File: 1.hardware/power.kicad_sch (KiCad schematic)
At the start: 45 parts, among them IC1 TPS7A2033PDBVR, IC4 TPS7A2018PDBVR, IC5 LMR14030SDDAR, J4 12V~24V BAT, J5 12V-24V Jack

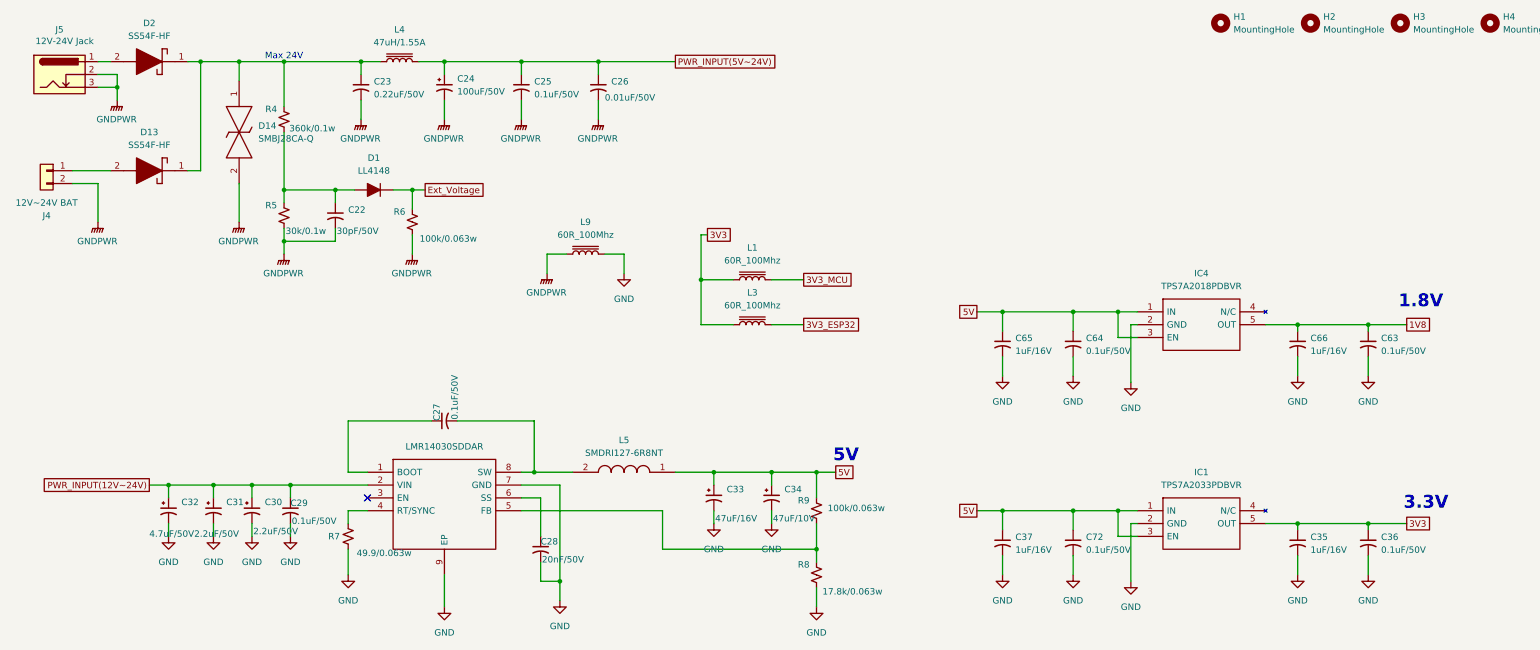
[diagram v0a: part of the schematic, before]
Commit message: 스펙 변경 12~48V 인풋 + 모스펫 구동에 필요한 전압 구현 필요
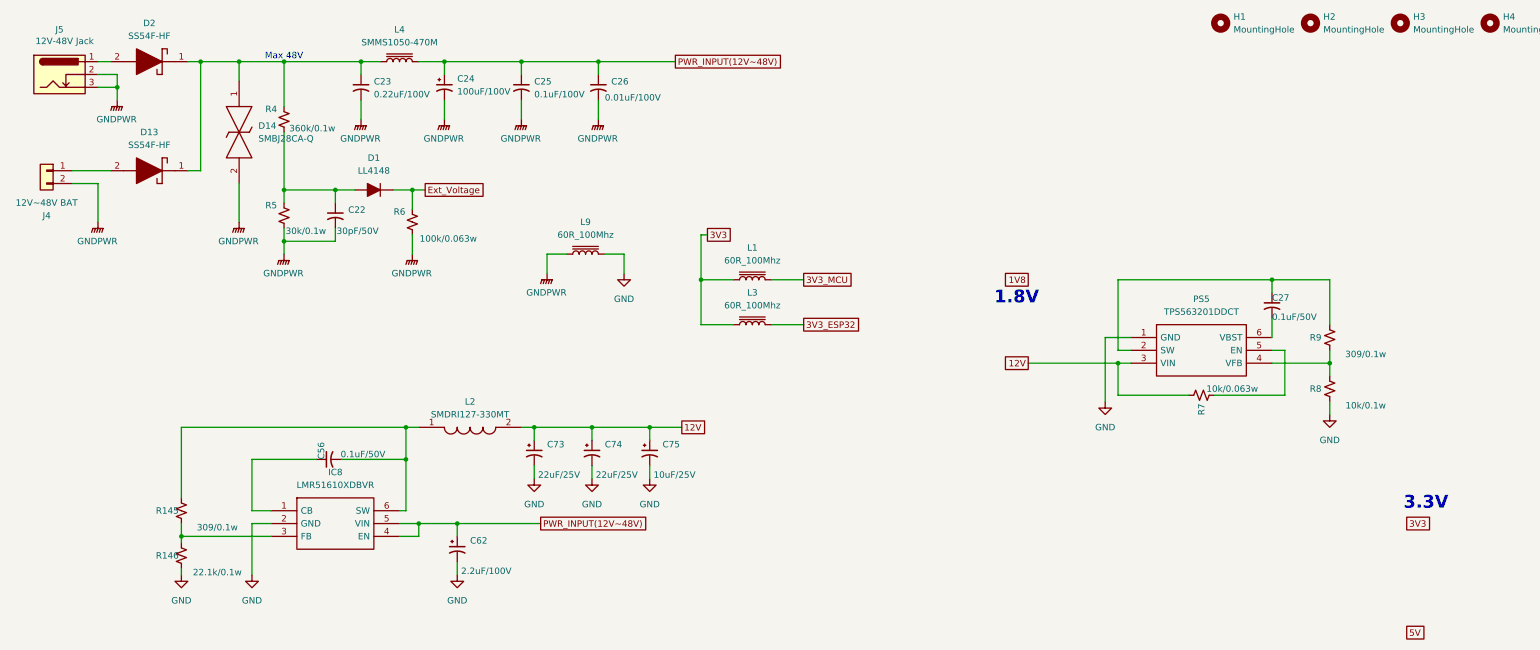
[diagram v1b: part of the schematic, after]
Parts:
- removed C28: 20nF/50V, Capacitor_SMD:C_0402_1005Metric, symbol Device:C_Small_US
- removed C29, C36, C63, C64, C72: 0.1uF/50V, Capacitor_SMD:C_0402_1005Metric, symbol Device:C_Small_US
- removed C30, C31: 2.2uF/50V, symbol Device:C_Polarized_Small_US
- removed C32: 4.7uF/50V, symbol Device:C_Polarized_Small_US
- removed C33: 47uF/16V, symbol Device:C_Polarized_Small_US
- removed C34: 47uF/10V, symbol Device:C_Polarized_Small_US
- removed C35, C37, C65, C66: 1uF/16V, Capacitor_SMD:C_0402_1005Metric, symbol Device:C_Small_US
- removed IC1: TPS7A2033PDBVR, SOT95P280X145-5N, symbol SamacSys_Parts:TPS7A2033PDBVR
- removed IC4: TPS7A2018PDBVR, SamacSys_Parts:SOT95P280X145-5N, symbol SamacSys_Parts:TPS7A20185PDBVR
- removed IC5: LMR14030SDDAR, SOIC127P600X170-9N, symbol SamacSys_Parts:LMR14030SDDAR
- removed L5: SMDRI127-6R8NT, SMDRI1276R8NT, symbol SamacSys_Parts:SMDRI127-6R8NT
- added C56: 0.1uF/50V, Capacitor_SMD:C_0402_1005Metric, symbol Device:C_Small_US
- added C62: 2.2uF/100V, symbol Device:C_Polarized_Small_US
- added C73, C74: 22uF/25V, symbol Device:C_Polarized_Small_US
- added C75: 10uF/25V, symbol Device:C_Polarized_Small_US
- added IC8: LMR51610XDBVR, SOT95P280X145-6N, symbol SamacSys_Parts:LMR51610XDBVR
- added L2: SMDRI127-330MT, SMDRI127330MT, symbol SamacSys_Parts:SMDRI127-330MT
- added PS5: TPS563201DDCT, SOT95P280X110-6N, symbol SamacSys_Parts:TPS563201DDCT
- added R145: 309/0.1w, symbol Device:R_Small_US
- added R146: 22.1k/0.1w, symbol Device:R_Small_US
- C23: value 0.22uF/50V -> 0.22uF/100V
- C24: value 100uF/50V -> 100uF/100V
- C25: value 0.1uF/50V -> 0.1uF/100V
- C26: value 0.01uF/50V -> 0.01uF/100V
- J4: value 12V~24V BAT -> 12V~48V BAT
- J5: value 12V-24V Jack -> 12V-48V Jack
- L4: value 47uH/1.55A -> SMMS1050-470M
- R7: value 49.9/0.063w -> 10k/0.063w
- R8: value 17.8k/0.063w -> 10k/0.1w
- R9: value 100k/0.063w -> 309/0.1w
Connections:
- net 5V: no longer R9.2
- net GND: now also C62.2, C73.2, C74.2, C75.2, IC8.2 (GND), PS5.1 (GND), R146.1; no longer R7.1
- net at C27.2: now also PS5.6 (VBST)
- net at C27.1: now also R9.2, PS5.2 (SW)
- net 12V: now reaches R7.2
- net 12V: now also C73.1, C74.1, C75.1, L2.2, PS5.3 (VIN)
- net at R8.2, R9.1: now also PS5.4 (VFB)
- net PWR_INPUT(5V~24V) renamed PWR_INPUT(12V~48V)
- net PWR_INPUT(12V~48V): now also C62.1, IC8.4 (EN), IC8.5 (VIN)
- new net: PS5.5 (EN), R7.1
- new net: C56.1, IC8.1 (CB)
- new net: C56.2, IC8.6 (SW), L2.1, R145.2
- new net: IC8.3 (FB), R145.1, R146.2
- no-connect marks 1 -> 0
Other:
- note added: "Max 48V"
- note removed: "5V"
- note removed: "Max 24V"

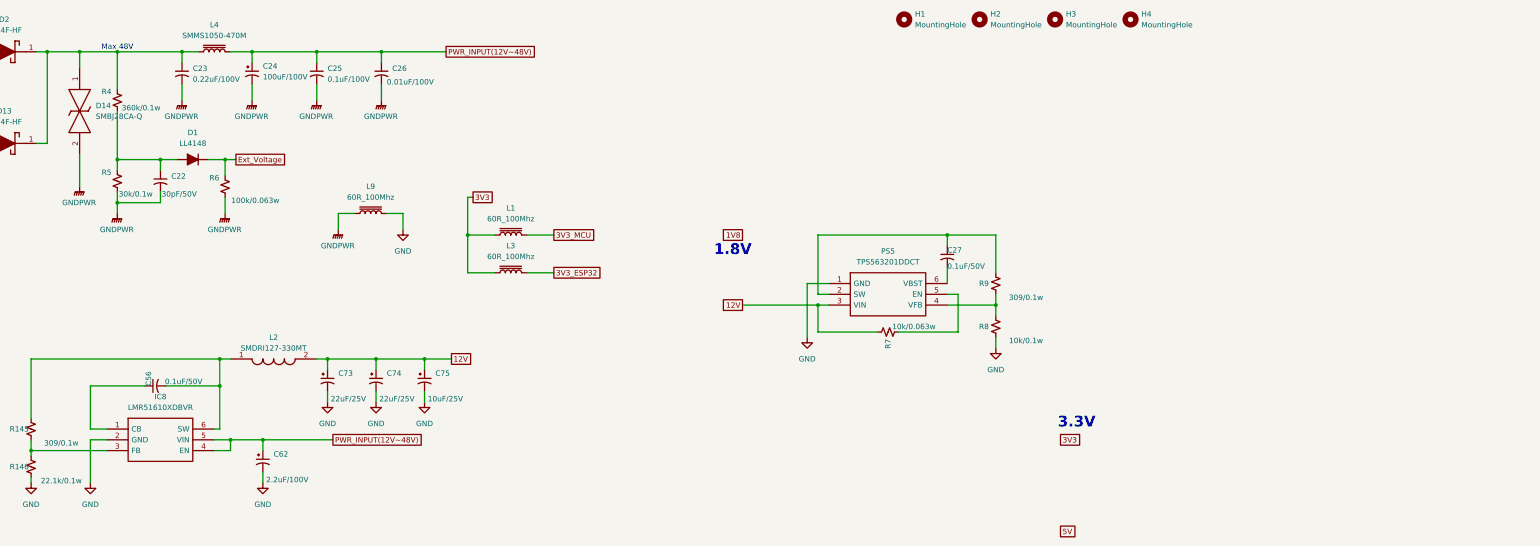
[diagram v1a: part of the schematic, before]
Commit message: mosfet 확정 및 드라이버 고려중 자세한 계산식 필요
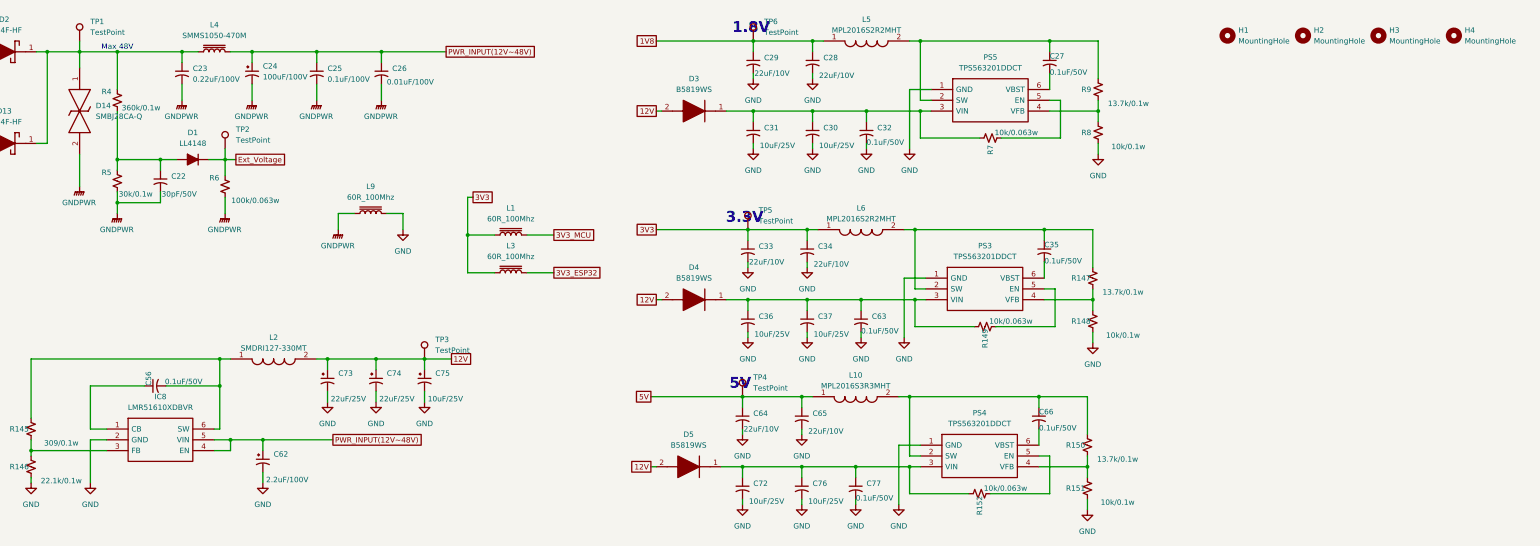
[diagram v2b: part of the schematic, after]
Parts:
- added C28, C29, C33, C34, C64, C65: 22uF/10V, Capacitor_SMD:C_0603_1608Metric, symbol Device:C_Small_US
- added C30, C31, C36, C37, C72, C76: 10uF/25V, Capacitor_SMD:C_0603_1608Metric, symbol Device:C_Small_US
- added C32, C63, C77: 0.1uF/50V, Capacitor_SMD:C_0603_1608Metric, symbol Device:C_Small_US
- added C35, C66: 0.1uF/50V, Capacitor_SMD:C_0402_1005Metric, symbol Device:C_Small_US
- added D3, D4, D5: B5819WS, SOD2613X100N, symbol SamacSys_Parts:B5819WS
- added L10: MPL2016S3R3MHT, SamacSys_Parts:INDC2116X100N, symbol SamacSys_Parts:MPL2016S2R2MHT
- added L5, L6: MPL2016S2R2MHT, SamacSys_Parts:INDC2116X100N, symbol SamacSys_Parts:MPL2016S2R2MHT
- added PS3, PS4: TPS563201DDCT, SamacSys_Parts:SOT95P280X110-6N, symbol SamacSys_Parts:TPS563201DDCT
- added R147, R150: 13.7k/0.1w, symbol Device:R_Small_US
- added R148, R151: 10k/0.1w, symbol Device:R_Small_US
- added R149, R152: 10k/0.063w, symbol Device:R_Small_US
- added TP1, TP2, TP3, TP4, TP5, TP6: TestPoint, symbol Connector:TestPoint
- D13, D2: footprint SODFL4626X120N -> SamacSys_Parts:SODFL4626X120N
- D14: footprint DIONM5436X244N -> SamacSys_Parts:DIONM5436X244N
- PS5: footprint SOT95P280X110-6N -> SamacSys_Parts:SOT95P280X110-6N
- R9: value 309/0.1w -> 13.7k/0.1w
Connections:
- net 12V: now also D3.2, D4.2, D5.2, TP3.1; no longer PS5.3 (VIN), R7.2
- net 1V8: now also C28.1, C29.1, L5.1, TP6.1
- net 3V3: now also C33.1, C34.1, L6.1, TP5.1
- net 5V: now also C64.1, C65.1, L10.1, TP4.1
- net Ext_Voltage: now also TP2.1
- net GND: now also C28.2, C29.2, C30.2, C31.2, C32.2, C33.2, C34.2, C36.2, C37.2, C63.2, C64.2, C65.2, C72.2, C76.2, C77.2, PS3.1 (GND), PS4.1 (GND), R148.1, R151.1
- net at C23.1, D13.1, D14.1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: now also TP1.1
- net at C27.1, PS5.2 (SW), R9.2: now also L5.2
- new net: C35.1, L6.2, PS3.2 (SW), R147.2
- new net: C36.1, C37.1, C63.1, D4.1, PS3.3 (VIN), R149.2
- new net: PS3.4 (VFB), R147.1, R148.2
- new net: PS3.5 (EN), R149.1
- new net: C35.2, PS3.6 (VBST)
- new net: C66.1, L10.2, PS4.2 (SW), R150.2
- new net: C30.1, C31.1, C32.1, D3.1, PS5.3 (VIN), R7.2
- new net: PS4.4 (VFB), R150.1, R151.2
- new net: PS4.5 (EN), R152.1
- new net: C72.1, C76.1, C77.1, D5.1, PS4.3 (VIN), R152.2
- new net: C66.2, PS4.6 (VBST)
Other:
- note added: "5V"
- moved on the sheet: C27, H1, H2, H3, H4, PS5, R7, R8, R9

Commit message: 중간 저장
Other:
- note added: "12V"
- moved on the sheet: C27, C28, C29, C30, C31, C32, C64, C65, C66, C72, C76, C77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

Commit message: 중간저장
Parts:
- removed D13, D2: SS54F-HF, SamacSys_Parts:SODFL4626X120N, symbol SamacSys_Parts:SS54F-HF
- removed D14: SMBJ28CA-Q, SamacSys_Parts:DIONM5436X244N, symbol SamacSys_Parts:SMBJ28CA-Q
- added D13: SMBJ54CA-Q, DIONM5436X244N, symbol SamacSys_Parts:SMBJ54CA-Q
- added D2, D6: SS58c, Diode_SMD:D_SMC, symbol PCM_Diode_Schottky_AKL:D_Schottky_Generic
- added SW1: SW_DPST_x2, symbol Switch:SW_DPST_x2
- TP1: value TestPoint -> TP_V_input
- TP3: value TestPoint -> TP_12V
- TP4: value TestPoint -> TP_5V
- TP5: value TestPoint -> TP_3V3
- TP6: value TestPoint -> TP_1V8
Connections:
- net GNDPWR: now also D13.2
- net at C23.1, L4.1, R4.2: now also D13.1, SW1.2 (B); no longer TP1.1
- net at J5.1: now also D6.2 (A)
- net at J4.1 (Pin_1): now also D2.2 (A)
- new net: D2.1 (K), D6.1 (K), SW1.1 (A), TP1.1
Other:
- moved on the sheet: C22, C23, C24, C25, C26, C56, C62, C73, C74, C75, D1, IC8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

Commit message: 중간 저장
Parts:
- removed D1: LL4148, PCM_Diode_SMD_AKL:D_MiniMELF, symbol PCM_Diode_AKL:LL4148
- added D1: B5819WS, SOD2613X100N, symbol SamacSys_Parts:B5819WS
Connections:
- net Ext_Voltage: now also D1.1
- net at C22.1, R4.1, R5.2: now also D1.2
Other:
- moved on the sheet: R6, TP2
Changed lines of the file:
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@@
 	)
 	(junction
-		(at 116.84 55.88)
+		(at 124.46 55.88)
 		(diameter 0)
 		(color 0 0 0 0)
@@
 	(wire
 		(pts
-			(xy 113.03 55.88) (xy 116.84 55.88)
+			(xy 120.65 55.88) (xy 124.46 55.88)
 		)
 		(stroke
@@
 	(wire
 		(pts
-			(xy 116.84 55.88) (xy 116.84 59.69)
+			(xy 124.46 55.88) (xy 124.46 59.69)
 		)
 		(stroke
@@
 	(wire
 		(pts
-			(xy 116.84 53.34) (xy 116.84 55.88)
+			(xy 124.46 53.34) (xy 124.46 55.88)
 		)
 		(stroke
@@
 	(wire
 		(pts
-			(xy 116.84 64.77) (xy 116.84 68.58)
+			(xy 124.46 64.77) (xy 124.46 68.58)
 		)
 		(stroke
@@
 	(wire
 		(pts
-			(xy 116.84 55.88) (xy 119.38 55.88)
+			(xy 124.46 55.88) (xy 127 55.88)
 		)
 		(stroke
@@
 	(global_label "Ext_Voltage"
 		(shape passive)
-		(at 119.38 55.88 0)
+		(at 127 55.88 0)
 		(fields_autoplaced yes)
 		(effects
@@
 		)
 		(property "Intersheetrefs" "${INTERSHEET_REFS}"
-			(at 132.1394 55.88 0)
+			(at 139.7594 55.88 0)
 			(effects
 				(font
@@
 	)
 	(symbol
+		(lib_id "SamacSys_Parts:B5819WS")
+		(at 120.65 55.88 180)
+		(unit 1)
+		(exclude_from_sim no)
+		(in_bom yes)
+		(on_board yes)
+		(dnp no)
+		(fields_autoplaced yes)
+		(property "Reference" "D1"
+			(at 113.03 48.26 0)
+			(effects
+				(font
+					(size 1.27 1.27)
+				)
+			)
+		)
+		(property "Value" "B5819WS"
+			(at 113.03 50.8 0)
+			(effects
+				(font
+					(size 1.27 1.27)
+				)
+			)
+		)
+		(property "Footprint" "SOD2613X100N"
+			(at 109.22 55.88 0)
+			(effects
+				(font
+					(size 1.27 1.27)
+				)
+				(justify left)
+				(hide yes)
+			)
+		)
+		(property "Datasheet" "https://www.21yangjie.com/ggs/xxh/xxhxtdejg/B5817WS%20THRU%20B5819WS-SOD-323-%E6%B5%B7%E9%B8%A5%E8%84%9A.pdf"
+			(at 109.22 53.34 0)
+			(effects
+				(font
+					(size 1.27 1.27)
+				)
+				(justify left)
+				(hide yes)
+			)
+		)
+		(property "Description" "DIODE SCHOTTKY 40V 1A SOD323"
+			(at 120.65 55.88 0)
+			(effects
+				(font
+					(size 1.27 1.27)
+				)
+				(hide yes)
+			)
+		)
+		(property "Description_1" "DIODE SCHOTTKY 40V 1A SOD323"
+			(at 109.22 50.8 0)
+			(effects
+				(font
+					(size 1.27 1.27)
+				)
+				(justify left)
+				(hide yes)
+			)
+		)
+		(property "Height" "1"
+			(at 109.22 48.26 0)
+			(effects
+				(font
+					(size 1.27 1.27)
+				)
+				(justify left)
+				(hide yes)
+			)
+		)
+		(property "Manufacturer_Name" "Yangzhou Yangjie Electronic Technology Co., Ltd."
+			(at 109.22 45.72 0)
+			(effects
+				(font
+					(size 1.27 1.27)
+				)
+				(justify left)
+				(hide yes)
+			)
+		)
+		(property "Manufacturer_Part_Number" "B5819WS"
+			(at 109.22 43.18 0)
+			(effects
+				(font
+					(size 1.27 1.27)
+				)
+				(justify left)
+				(hide yes)
+			)
+		)
+		(property "Mouser Part Number" ""
+			(at 109.22 40.64 0)
+			(effects
+				(font
+					(size 1.27 1.27)
+				)
+				(justify left)
+				(hide yes)
+			)
+		)
+		(property "Mouser Price/Stock" ""
+			(at 109.22 38.1 0)
+			(effects
+				(font
+					(size 1.27 1.27)
+				)
+				(justify left)
+				(hide yes)
+			)
+		)
+		(property "Arrow Part Number" ""
+			(at 109.22 35.56 0)
+			(effects
+				(font
+					(size 1.27 1.27)
+				)
+				(justify left)
+				(hide yes)
+			)
+		)
+		(property "Arrow Price/Stock" ""
+			(at 109.22 33.02 0)
+			(effects
+				(font
+					(size 1.27 1.27)
+				)
+				(justify left)
+				(hide yes)
+			)
+		)
+		(pin "2"
+		)
+		(pin "1"
+		)
+		(instances
+			(project "bldc_motor_controller"
+				(path "/a25adab6-a8c3-4e0e-8ba9-baac00aaa394/fa552ebf-4859-4df7-97cc-cc5957e0d3a3"
+					(reference "D1")
+					(unit 1)
+				)
+			)
+		)
+	)
+	(symbol
 		(lib_id "power:GNDPWR")
 		(at 78.74 62.23 0)
@@
 	)
 	(symbol
-		(lib_id "PCM_Diode_AKL:LL4148")
-		(at 109.22 55.88 0)
-		(unit 1)
-		(exclude_from_sim no)
-		(in_bom yes)
-		(on_board yes)
-		(dnp no)
-		(fields_autoplaced yes)
-		(property "Reference" "D1"
-			(at 109.22 49.53 0)
-			(effects
-				(font
-					(size 1.27 1.27)
-				)
-			)
-		)
-		(property "Value" "LL4148"
-			(at 109.22 52.07 0)
-			(effects
-				(font
-					(size 1.27 1.27)
-				)
-			)
-		)
-		(property "Footprint" "PCM_Diode_SMD_AKL:D_MiniMELF"
-			(at 109.22 55.88 0)
-			(effects
-				(font
-					(size 1.27 1.27)
-				)
-				(hide yes)
-			)
-		)
-		(property "Datasheet" "https://www.tme.eu/Document/968b88464c4f5d5ff32cd1ca930873a4/LL4148-4448.pdf"
-			(at 109.22 55.88 0)
-			(effects
-				(font
-					(size 1.27 1.27)
-				)
-				(hide yes)
-			)
-		)
-		(property "Description" "MiniMELF Diode, Small Signal, Fast Switching, 75V, 150mA, 4ns, Alternate KiCad Library"
-			(at 109.22 55.88 0)
-			(effects
-				(font
-					(size 1.27 1.27)
-				)
-				(hide yes)
-			)
-		)
-		(pin "1"
-		)
-		(pin "2"
-		)
-		(instances
-			(project ""
-				(path "/a25adab6-a8c3-4e0e-8ba9-baac00aaa394/fa552ebf-4859-4df7-97cc-cc5957e0d3a3"
-					(reference "D1")
-					(unit 1)
-				)
-			)
-		)
-	)
-	(symbol
 		(lib_id "Device:L_Iron")
 		(at 162.56 127 90)
@@
 	(symbol
 		(lib_id "Device:R_Small_US")
-		(at 116.84 62.23 180)
+		(at 124.46 62.23 180)
 		(unit 1)
 		(exclude_from_sim no)
@@
 		(dnp no)
 		(property "Reference" "R6"
-			(at 114.3 60.198 0)
+			(at 121.92 60.198 0)
 			(effects
 				(font
@@
 		)
 		(property "Value" "100k/0.063w"
-			(at 123.952 65.532 0)
+			(at 131.572 65.532 0)
 			(effects
 				(font
@@
 		)
 		(property "Footprint" ""
-			(at 116.84 62.23 0)
+			(at 124.46 62.23 0)
 			(effects
 				(font
@@
 		)
 		(property "Datasheet" "~"
-			(at 116.84 62.23 0)
+			(at 124.46 62.23 0)
 			(effects
 				(font
@@
 		)
 		(property "Description" "Resistor, small US symbol"
-			(at 116.84 62.23 0)
+			(at 124.46 62.23 0)
 			(effects
 				(font
@@
 	(symbol
 		(lib_id "Connector:TestPoint")
-		(at 116.84 53.34 0)
+		(at 124.46 53.34 0)
 		(unit 1)
 		(exclude_from_sim no)
@@
 		(fields_autoplaced yes)
 		(property "Reference" "TP2"
-			(at 119.38 48.7679 0)
+			(at 127 48.7679 0)
 			(effects
 				(font
@@
 		)
 		(property "Value" "TestPoint"
-			(at 119.38 51.3079 0)
+			(at 127 51.3079 0)
 			(effects
 				(font
@@
 		)
 		(property "Footprint" ""
-			(at 121.92 53.34 0)
+			(at 129.54 53.34 0)
 			(effects
 				(font
@@
 		)
 		(property "Datasheet" "~"
-			(at 121.92 53.34 0)
+			(at 129.54 53.34 0)
 			(effects
 				(font
@@
 		)
 		(property "Description" "test point"
-			(at 116.84 53.34 0)
+			(at 124.46 53.34 0)
 			(effects
 				(font
@@
 	(symbol
 		(lib_id "power:GNDPWR")
-		(at 116.84 68.58 0)
+		(at 124.46 68.58 0)
 		(unit 1)
 		(exclude_from_sim no)
@@
 		(fields_autoplaced yes)
 		(property "Reference" "#PWR024"
-			(at 116.84 73.66 0)
+			(at 124.46 73.66 0)
 			(effects
 				(font
@@
 		)
 		(property "Value" "GNDPWR"
-			(at 116.713 72.39 0)
+			(at 124.333 72.39 0)
 			(effects
 				(font
@@
 		)
 		(property "Footprint" ""
-			(at 116.84 69.85 0)
+			(at 124.46 69.85 0)
 			(effects
 				(font
@@
 		)
 		(property "Datasheet" ""
-			(at 116.84 69.85 0)
+			(at 124.46 69.85 0)
 			(effects
 				(font
@@
 		)
 		(property "Description" "Power symbol creates a global label with name \"GNDPWR\" , global ground"
-			(at 116.84 68.58 0)
+			(at 124.46 68.58 0)
 			(effects
 				(font
